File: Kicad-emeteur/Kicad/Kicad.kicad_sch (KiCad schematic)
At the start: 26 parts, among them J1 Conn_02x07_Odd_Even, J2 Conn_01x02, J5 Conn_01x02, J52 Conn_01x04, J6 Conn_01x03, J62 Conn_01x03, U1 STM32L021K4Tx, U2 BU33SD5WG-TR

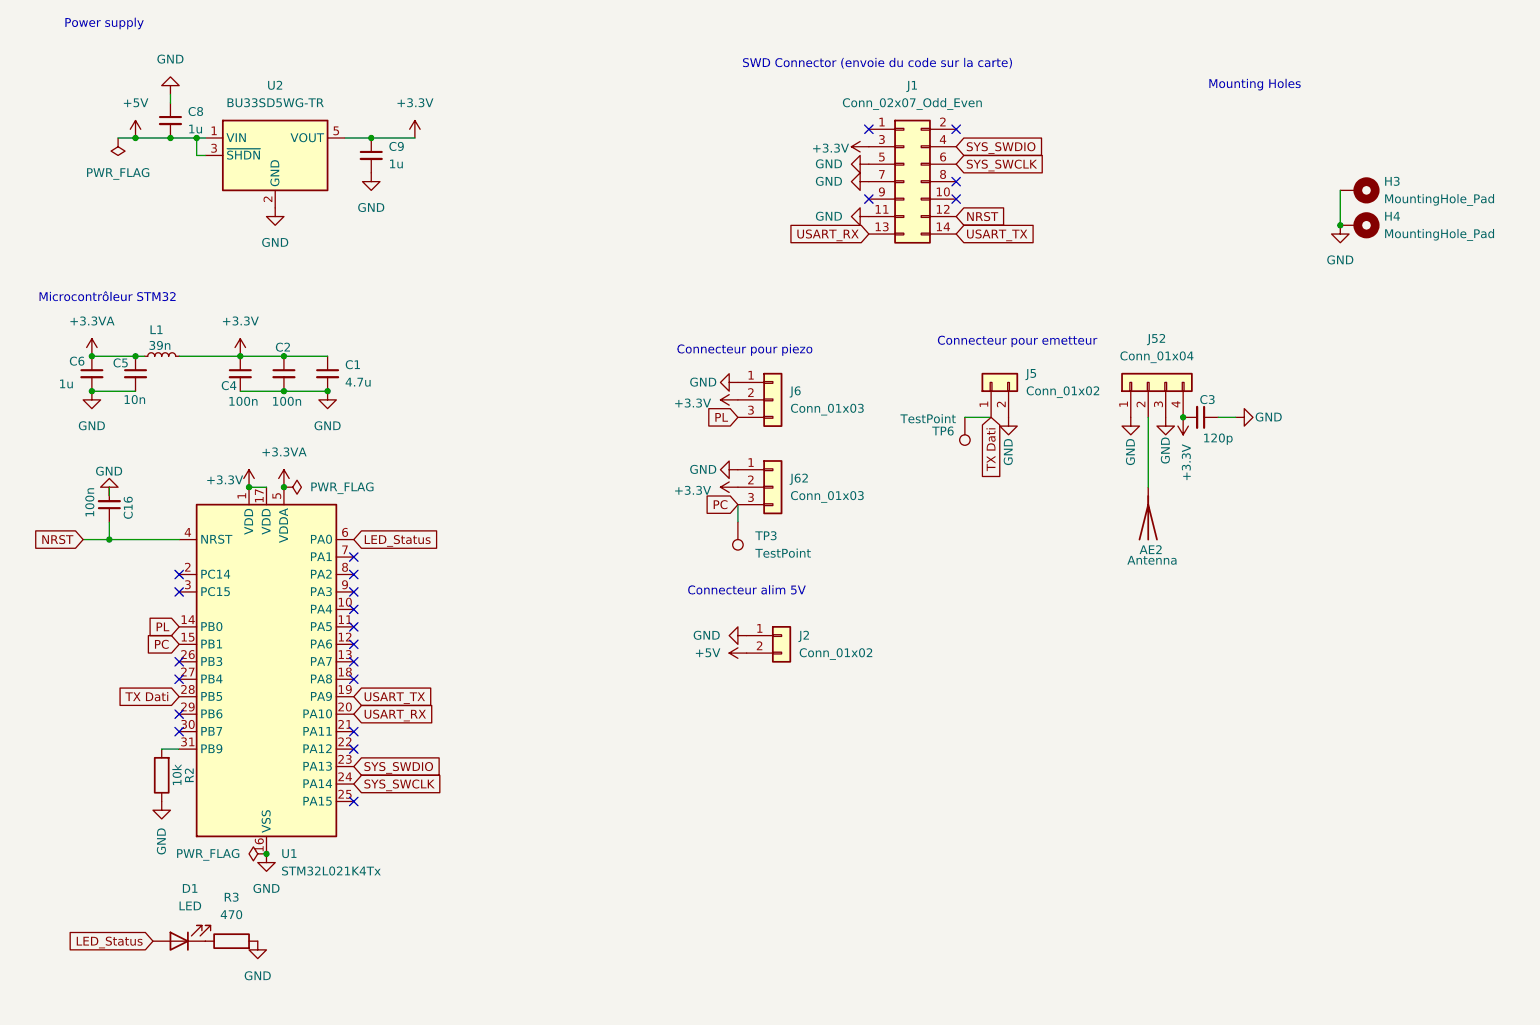
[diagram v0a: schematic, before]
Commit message: feat: Add initial KiCad project files for emitter and receiver modules.
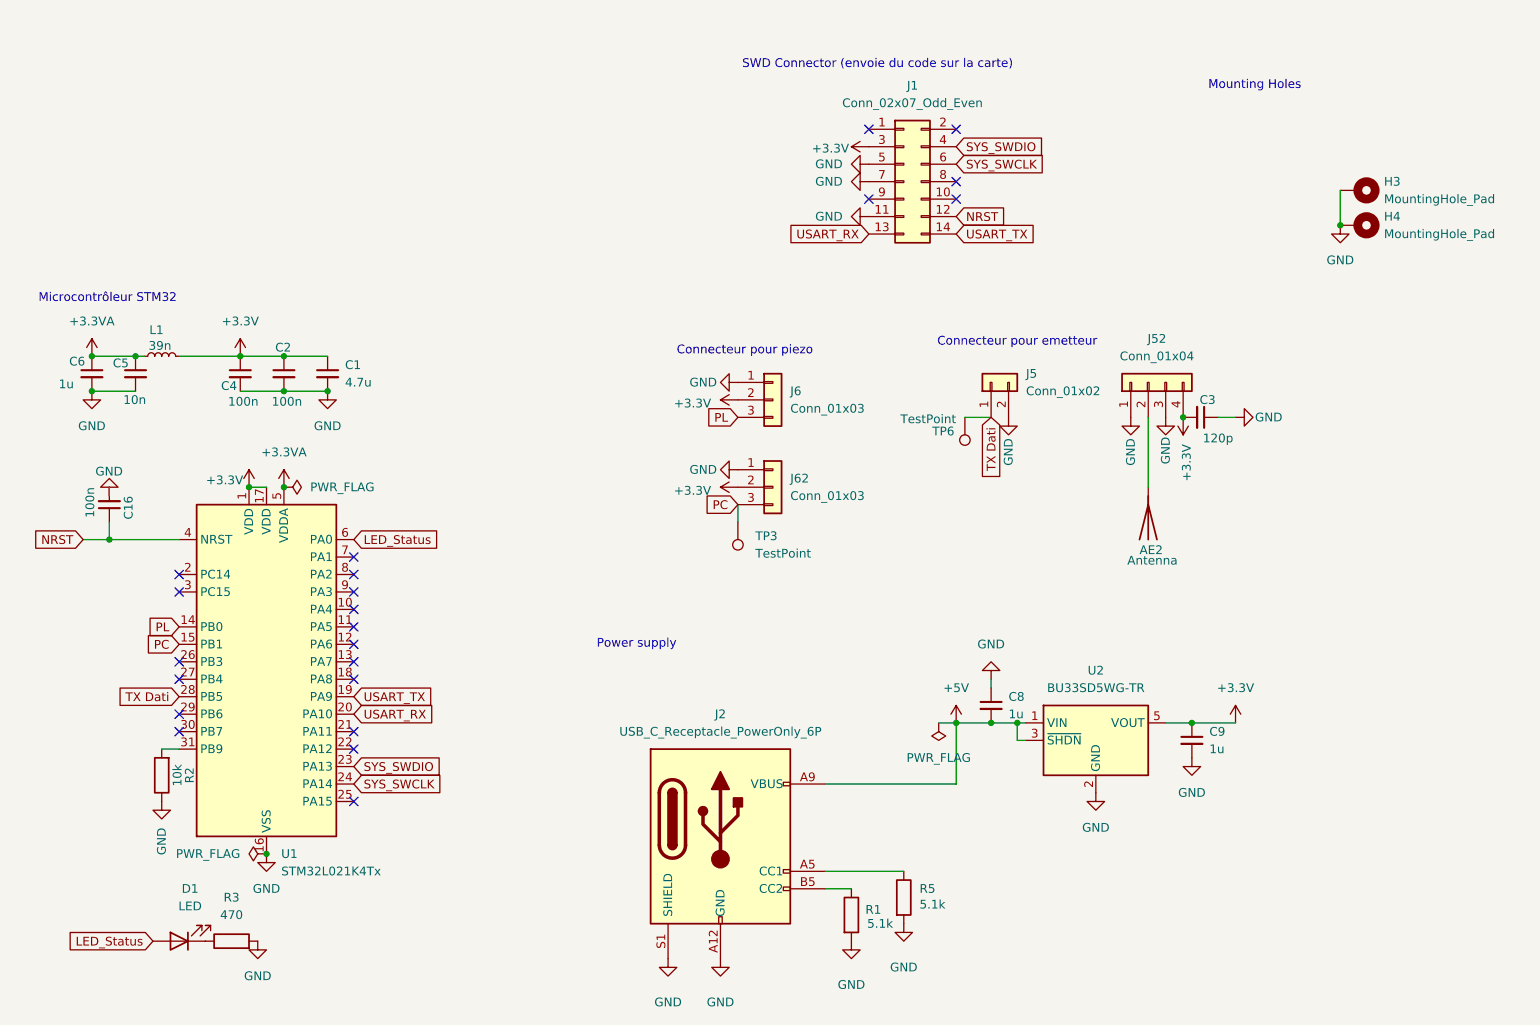
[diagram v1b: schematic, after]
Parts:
- removed J2: Conn_01x02, Connector_PinSocket_2.54mm:PinSocket_1x02_P2.54mm_Vertical, symbol Connector_Generic:Conn_01x02
- added J2: USB_C_Receptacle_PowerOnly_6P, Connector_USB:USB_C_Receptacle_GCT_USB4125-xx-x-0190_6P_TopMnt_Horizontal, symbol Connector:USB_C_Receptacle_PowerOnly_6P
- added R1, R5: 5.1k, Resistor_SMD:R_0603_1608Metric_Pad0.98x0.95mm_HandSolder, symbol Device:R
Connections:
- net +5V: now also J2.A9 (VBUS), J2.B9 (VBUS)
- net GND: now also J2.A12 (GND), J2.B12 (GND), J2.S1 (SHIELD), R1.2, R5.2
- new net: J2.B5 (CC2), R1.1
- new net: J2.A5 (CC1), R5.1
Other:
- note removed: "Connecteur alim 5V"
- moved on the sheet: C8, C9, U2
